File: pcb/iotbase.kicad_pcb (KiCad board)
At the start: 2 copper layers, 57 x 72.5 mm, 38 parts, among them J1 USB_C_Receptacle_USB2.0, J2 RCWL-0516, J3 HSPI, J4 VSPI, SW1 Reset, SW2 Boot, U1 BME280, U2 AMS1117-3.3, U3 Connector_I2C, U4 Connector_I2C, U5 ESP32-WROOM-E, U6 Connector_IoT_GPIO, U7 Connector_ESProg, U8 HDC1080

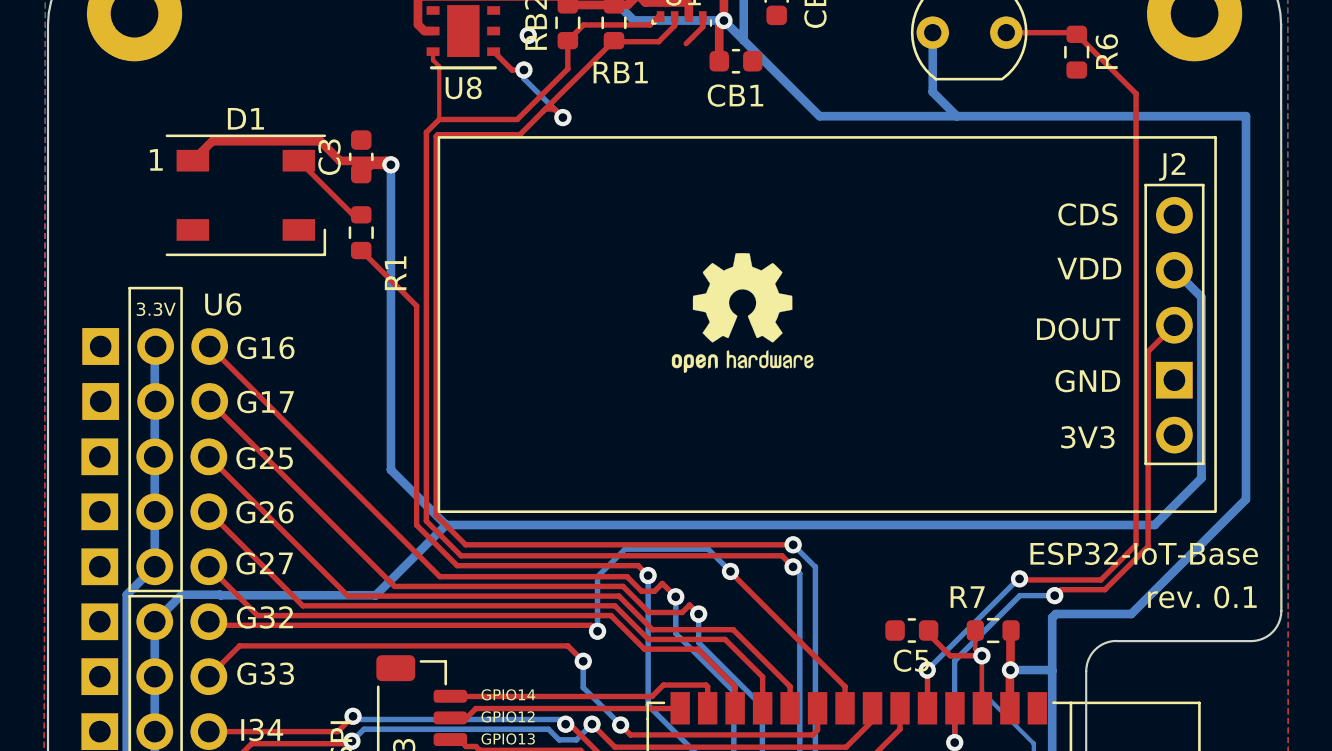
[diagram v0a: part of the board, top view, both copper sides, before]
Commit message: connects WS2812 led to 3.3v, fixes #3
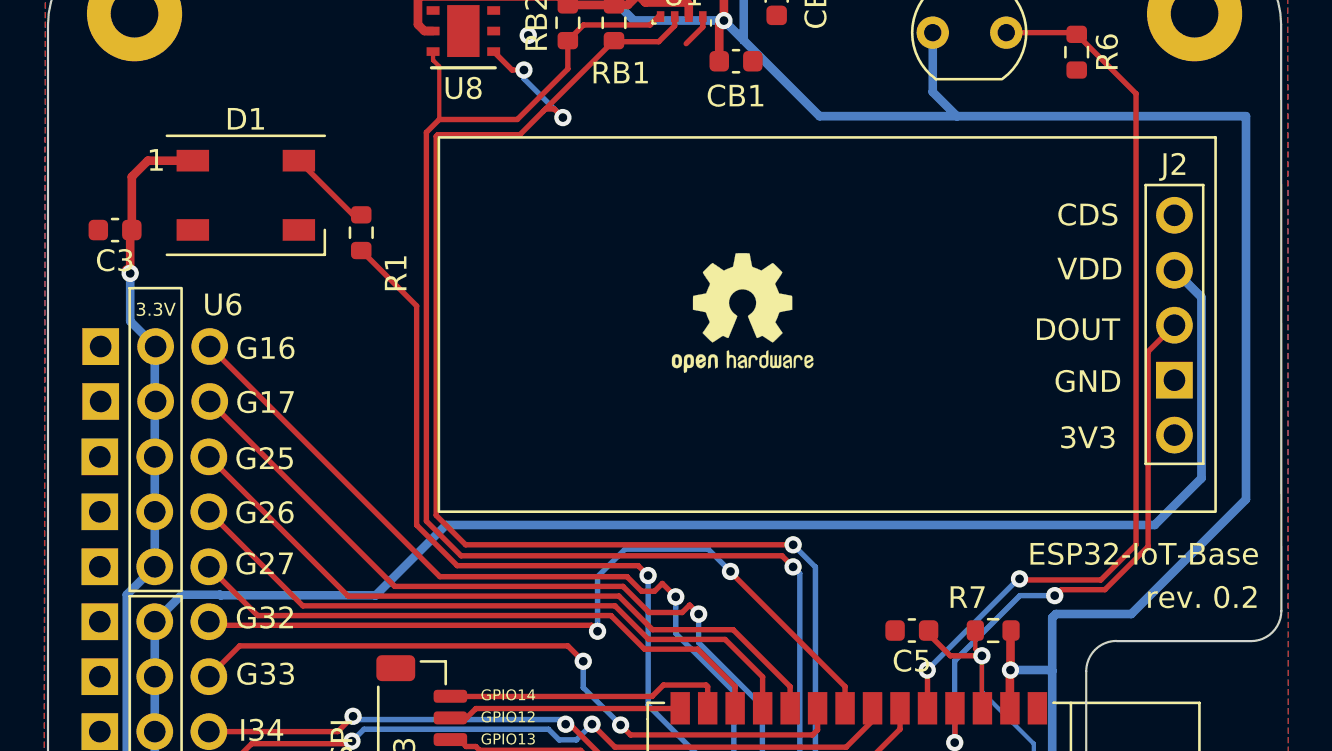
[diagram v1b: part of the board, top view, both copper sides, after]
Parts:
- moved C3 11.9 mm to (92.1, 71.0), turned to 180 degrees
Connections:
- C3 pad 1: VBUS -> +3V3
- D1 pad 1: VBUS -> +3V3
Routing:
- net VBUS: track 165.4 -> 136.1 mm, vias 5 -> 4
- net +3V3: track 288.6 -> 300.4 mm, vias 10 -> 11
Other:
- board text added: "rev. 0.2"
- board text removed: "rev. 0.1"

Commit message: fixes boot issues by updating C5 to 10uf
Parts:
- C5: value 100nF -> 10uf

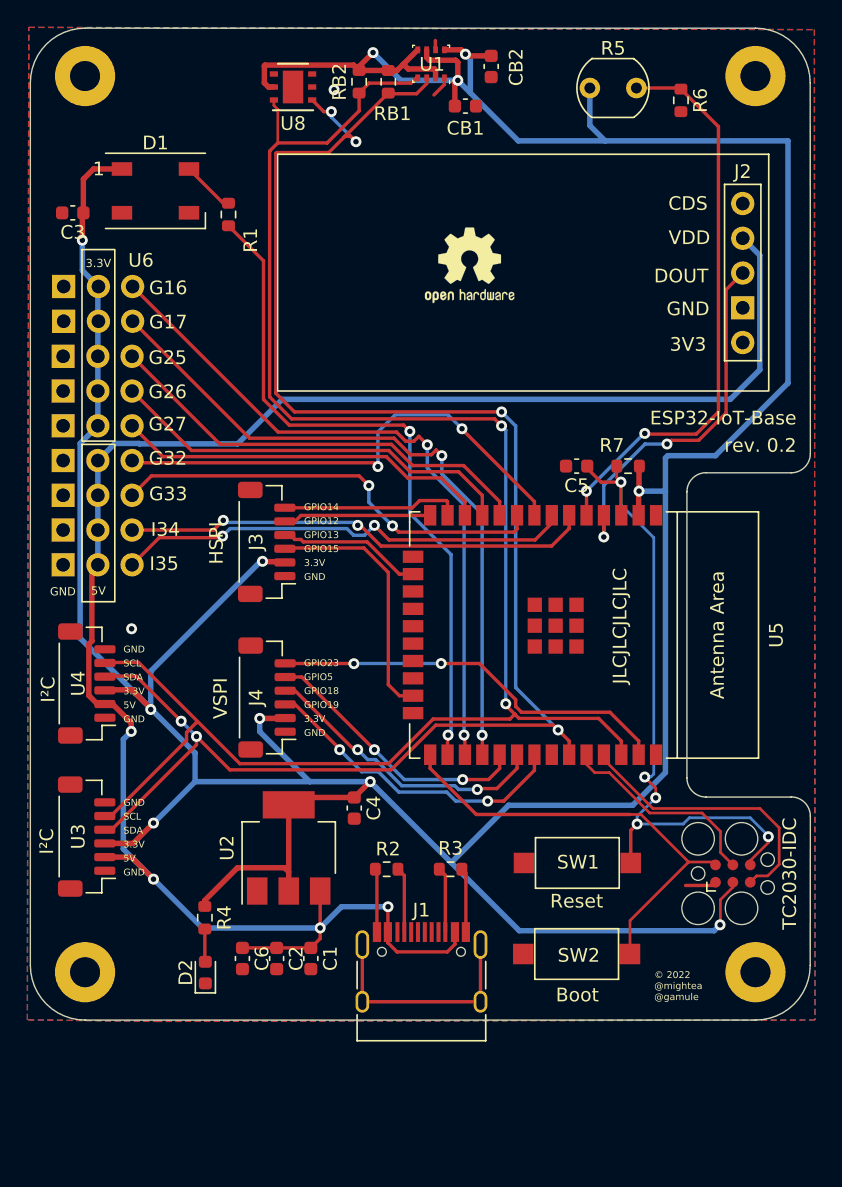
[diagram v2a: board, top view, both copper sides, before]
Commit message: reduced pcb size added header for RCWL-0516 removed BME280 to save on cost replaced buttons with solder pads
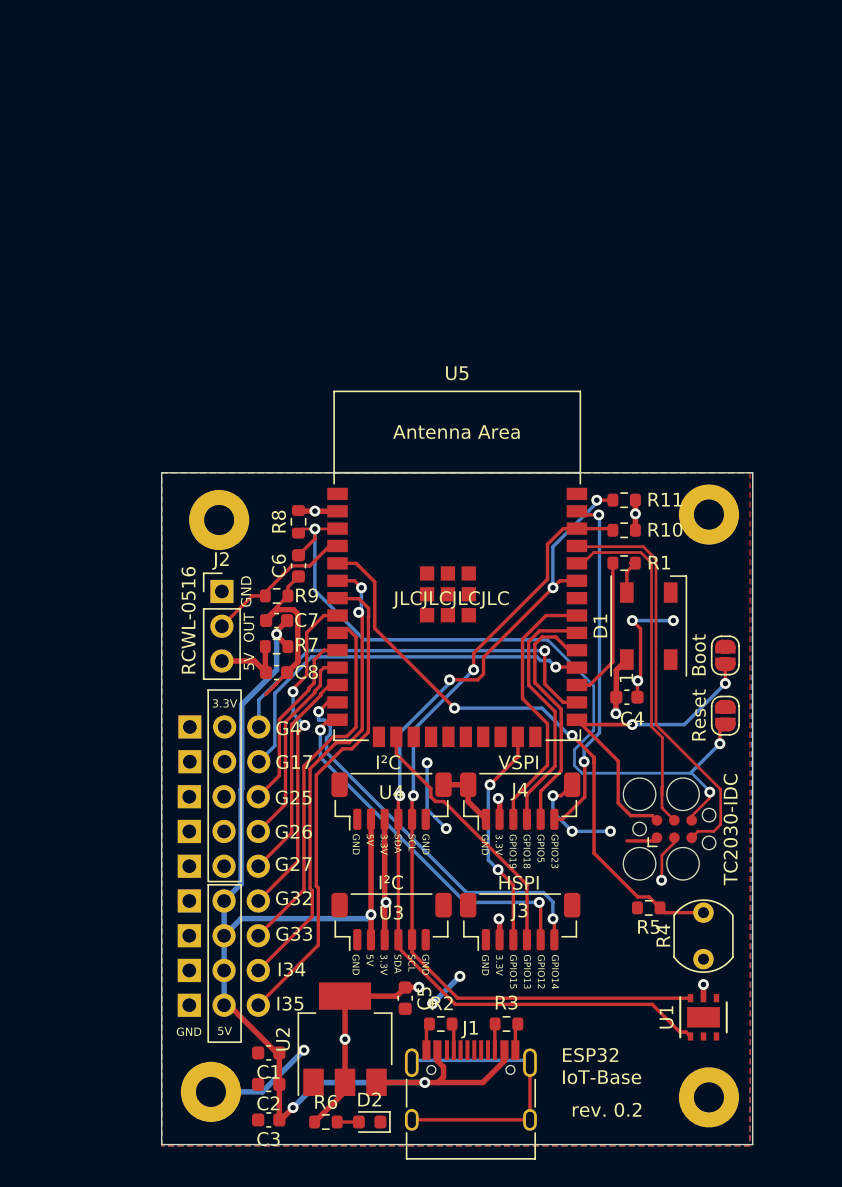
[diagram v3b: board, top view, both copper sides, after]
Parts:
- removed CB1, CB2: 100nF, Capacitor_SMD:C_0603_1608Metric
- removed REF**: OSHW-Logo2_7.3x6mm_SilkScreen, Symbol:OSHW-Logo2_7.3x6mm_SilkScreen
- removed SW1: Reset, Button_Switch_SMD:SW_SPST_CK_RS282G05A3
- removed SW2: Boot, Button_Switch_SMD:SW_SPST_CK_RS282G05A3
- removed the U1 at (118.3, 60.1)
- added C7: 1000uf, Capacitor_SMD:C_0603_1608Metric, F.Cu at (107.0, 100.8)
- added C8: 1000uf, Capacitor_SMD:C_0603_1608Metric, F.Cu at (107.0, 104.6)
- added JP1: Reset, Jumper:SolderJumper-2_P1.3mm_Open_RoundedPad1.0x1.5mm, F.Cu at (139.8, 107.8)
- added JP2: Boot, Jumper:SolderJumper-2_P1.3mm_Open_RoundedPad1.0x1.5mm, F.Cu at (139.8, 103.3)
- added R7: 10Ω, Resistor_SMD:R_0603_1608Metric, F.Cu at (107.0, 102.7)
- added R9: 10K, Resistor_SMD:R_0603_1608Metric, F.Cu at (107.0, 99.0)
- J2: footprint 0_Project:PinHeader_RCWL-0516 -> Connector_PinHeader_2.54mm:PinHeader_1x03_P2.54mm_Vertical
- moved U1 74.3 mm to (138.2, 129.8), turned to 90 degrees
- moved R4 64.2 mm to (138.2, 125.5), turned to 90 degrees
- moved R5 59.1 mm to (134.2, 121.8), turned to 180 degrees
- moved C4 53.8 mm to (132.6, 106.4), turned to 0 degrees
- moved D1 48.1 mm to (134.2, 101.2), turned to 90 degrees
- moved J2 47.5 mm to (103.0, 98.7)
- moved R1 38.5 mm to (132.4, 96.6), turned to 0 degrees
- moved R10 38.1 mm to (132.4, 94.2), turned to 0 degrees
- moved R11 35.1 mm to (132.4, 92.0), turned to 0 degrees
- moved H1 33.9 mm to (102.8, 93.5)
- moved U6 33.5 mm to (107.0, 105.4)
- moved J3 33.4 mm to (124.8, 122.8), turned to 0 degrees
- moved H2 32.2 mm to (138.6, 93.0)
- moved R8 24.4 mm to (108.6, 93.6), turned to -90 degrees
- moved U4 23.9 mm to (115.4, 114.0), turned to 0 degrees
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- renumbered C6 to C3, C3 to C4, C4 to C5, C5 to C6, RB2 to R10, RB1 to R11, R5 to R4, R6 to R5, R4 to R6, R7 to R8, U8 to U1
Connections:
- J2 pad 1: unconnected-(J2-Pad1) -> Net-(C8-Pad1)
- J2 pad 2: VBUS -> IO36
- J2 pad 3: IO36 -> GND
- R1 pad 1: GPIO4 -> GPIO16
- U6 pad 14: GPIO16 -> GPIO4
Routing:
- net +3V3: track 300.4 -> 41.9 mm, vias 11 -> 10
- net SCL: track 127.9 -> 60.8 mm
- net SDA: track 127.7 -> 67.3 mm, vias 6 -> 4
- net VBUS: track 136.1 -> 87.1 mm
- net GND: track 13.7 -> 57.9 mm, vias 2 -> 11
- net GPIO16: track 50.4 -> 10.5 mm, vias 2 -> 0
- net GPIO17: track 50.0 -> 29.0 mm, vias 2 -> 1
- net GPIO4: track 50.4 -> 29.7 mm, vias 2 -> 1
- net GPIO25: track 32.3 -> 13.7 mm
- net IO36: track 27.8 -> 11.0 mm, vias 2 -> 0
- net GPIO14: track 12.7 -> 29.2 mm, vias 0 -> 2
- net GPIO12: track 10.8 -> 26.8 mm, vias 0 -> 2
- net GPIO26: track 30.2 -> 15.0 mm
- net GPIO27: track 27.6 -> 16.0 mm
- net GPIO32: track 36.1 -> 25.1 mm
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- added copper zone on B.Cu, net +3V3
- removed copper zone on B.Cu, net GND
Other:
- board size 57 x 72.5 mm -> 43.2 x 49.1 mm
- board text added: "ESP32 IoT-Base"
- board text removed: "Boot"
- board text removed: "ESP32-IoT-Base"
- board text removed: "Reset"
- board text removed: "© 2022 @mightea @gamule"

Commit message: fixes drc warnings ads rounded corners to rev.2 updates changelog
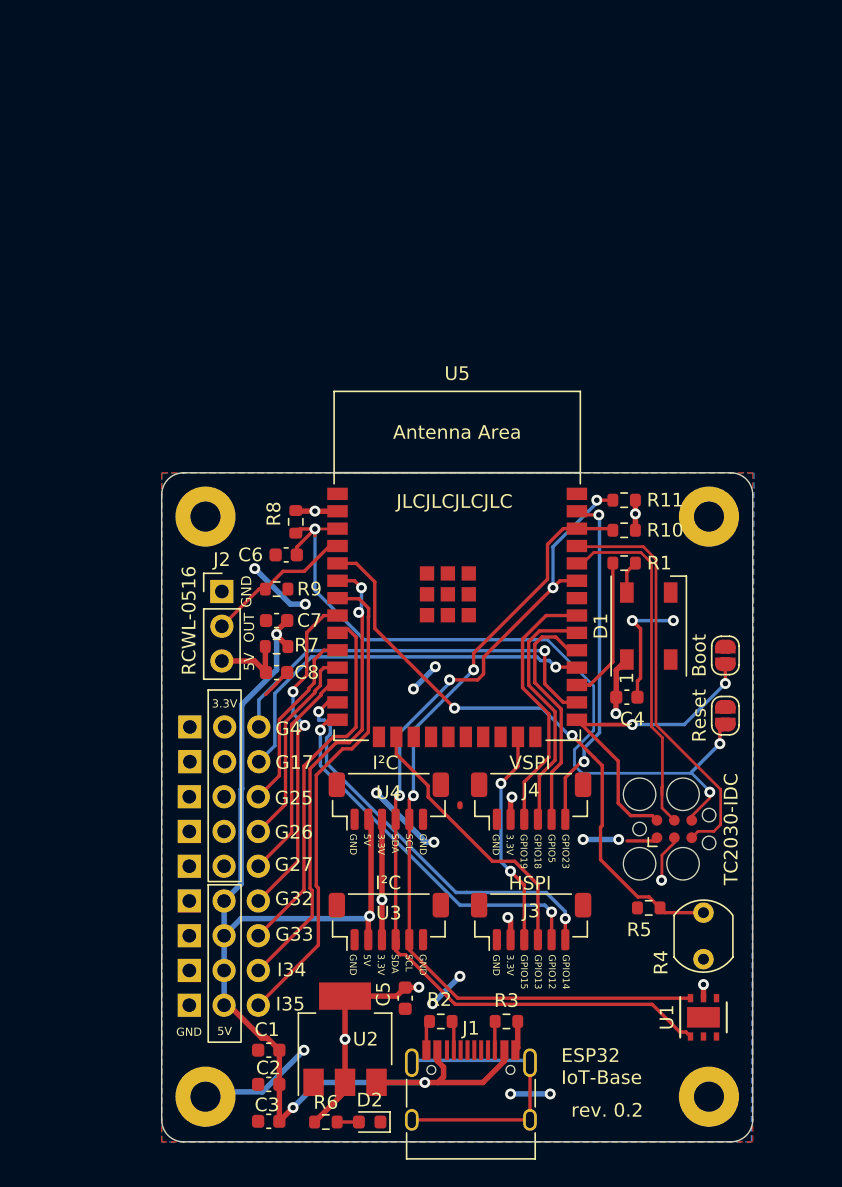
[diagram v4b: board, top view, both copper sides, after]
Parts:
- added REF**: OSHW-Logo2_9.8x8mm_SilkScreen, Symbol:OSHW-Logo2_9.8x8mm_SilkScreen, B.Cu at (133.4, 98.9)
- moved C6 1.20 mm to (107.7, 96.0), turned to 180 degrees
- moved H1 1.03 mm to (101.8, 93.2)
- moved J3 0.80 mm to (125.6, 122.8)
- moved J4 0.80 mm to (125.6, 114.0)
- moved H4 0.53 mm to (101.8, 135.6)
- moved R9 0.50 mm to (107.0, 98.5)
- moved C1 0.20 mm to (106.4, 132.2)
- moved U3 0.20 mm to (115.2, 122.8)
- moved U4 0.20 mm to (115.2, 114.0)
- moved R8 0.20 mm to (108.4, 93.6)
- moved R2 0.19 mm to (119.0, 130.1)
- moved R3 0.19 mm to (123.8, 130.1)
- moved H2 0.15 mm to (138.6, 93.2)
- moved C3 0.10 mm to (106.4, 137.4)
- moved H3 0.05 mm to (138.6, 135.6)
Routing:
- net GND: track 57.9 -> 47.5 mm, vias 11 -> 15
- net RESET: track 57.5 -> 58.7 mm
- net SDA: track 67.3 -> 68.4 mm
- net GPIO13: track 19.1 -> 20.1 mm
- net GPIO14: track 29.2 -> 30.0 mm
- net GPIO12: track 26.8 -> 27.6 mm
- net GPIO23: track 25.7 -> 25.1 mm
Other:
- board size 43.2 x 49.1 mm -> 43.2 x 48.9 mm
- board text added: "@mightea @gamule"
- board text added: "© 2022"

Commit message: updates jlcpcb compoent id's
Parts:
- removed REF**: OSHW-Logo2_9.8x8mm_SilkScreen, Symbol:OSHW-Logo2_9.8x8mm_SilkScreen
- C6: value 10uf -> 10uF
- C7, C8: value 1000uf -> 1000uF
- R10, R11: value 4.7 K -> 4.7 KΩ
- R2, R3, R6: value 4k7 -> 4.7 KΩ
- R8, R9: value 10K -> 10kΩ
